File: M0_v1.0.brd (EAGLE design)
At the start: 68.6 x 53.3 mm, 61 parts, among them CN1 POWER_JACK, CN2 47346-0001, CN3 DIGITAL10, CN4 DIGITAL8, CN5 ICSP, CN6 POWER8, CN7 ANALOG6, CN8 SWD, CN9 UART, IC1 AMS1117-5.0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

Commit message: Moved i2c lines away from usb lines to prevent interference.
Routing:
- net SCL: track 38.2 -> 33.5 mm
- net SDA: track 36.2 -> 31.6 mm
- net GND: vias 210 -> 211
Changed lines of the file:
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@@
 <via x="43.053" y="35.687" extent="1-16" drill="0.35"/>
 <via x="43.053" y="27.94" extent="1-16" drill="0.35"/>
-<via x="39.497" y="25.527" extent="1-16" drill="0.35"/>
+<via x="39.624" y="25.527" extent="1-16" drill="0.35"/>
 <via x="33.909" y="28.194" extent="1-16" drill="0.35"/>
 <via x="49.657" y="6.604" extent="1-16" drill="0.35"/>
 <via x="18.923" y="36.195" extent="1-16" drill="0.35"/>
 <via x="29.464" y="31.877" extent="1-16" drill="0.35"/>
-<via x="38.354" y="32.385" extent="1-16" drill="0.35"/>
-<via x="34.036" y="34.671" extent="1-16" drill="0.35"/>
-<via x="22.606" y="46.355" extent="1-16" drill="0.35"/>
-<via x="22.86" y="41.402" extent="1-16" drill="0.35"/>
-<via x="28.702" y="39.624" extent="1-16" drill="0.35"/>
-<via x="34.163" y="39.624" extent="1-16" drill="0.35"/>
-<via x="28.067" y="46.355" extent="1-16" drill="0.35"/>
-<via x="18.923" y="39.751" extent="1-16" drill="0.35"/>
+<via x="37.465" y="31.369" extent="1-16" drill="0.35"/>
+<via x="34.798" y="32.004" extent="1-16" drill="0.35"/>
+<via x="25.273" y="46.228" extent="1-16" drill="0.35"/>
+<via x="29.464" y="41.656" extent="1-16" drill="0.35"/>
+<via x="29.845" y="37.084" extent="1-16" drill="0.35"/>
+<via x="34.671" y="36.576" extent="1-16" drill="0.35"/>
+<via x="30.861" y="46.228" extent="1-16" drill="0.35"/>
+<via x="19.812" y="40.005" extent="1-16" drill="0.35"/>
 <via x="18.923" y="46.228" extent="1-16" drill="0.35"/>
-<via x="18.034" y="48.387" extent="1-16" drill="0.35"/>
+<via x="18.034" y="48.514" extent="1-16" drill="0.35"/>
 <via x="14.605" y="39.878" extent="1-16" drill="0.35"/>
 <via x="10.795" y="35.941" extent="1-16" drill="0.35"/>
@@
 <wire x1="49.09495" y1="31" x2="48.9808" y2="31.11415" width="0.3048" layer="1"/>
 <via x="54.356" y="4.826" extent="1-16" drill="0.35"/>
-<via x="33.401" y="44.704" extent="1-16" drill="0.35"/>
+<via x="34.417" y="42.545" extent="1-16" drill="0.35"/>
 <via x="61.595" y="42.926" extent="1-16" drill="0.35"/>
 <via x="12.827" y="25.273" extent="1-16" drill="0.35"/>
@@
 <via x="37.338" y="49.276" extent="1-16" drill="0.35"/>
 <via x="57.531" y="48.26" extent="1-16" drill="0.35"/>
-<via x="22.86" y="48.514" extent="1-16" drill="0.35"/>
+<via x="24.892" y="41.656" extent="1-16" drill="0.35"/>
 <via x="18.288" y="21.844" extent="1-16" drill="0.35"/>
 <via x="22.098" y="24.257" extent="1-16" drill="0.35"/>
@@
 <via x="43.18" y="23.241" extent="1-16" drill="0.35"/>
 <via x="55.499" y="31.242" extent="1-16" drill="0.35"/>
+<via x="22.987" y="48.641" extent="1-16" drill="0.35"/>
 </signal>
 <signal name="VIN" class="3">
@@
 <wire x1="58.4736" y1="45.1386" x2="40.1828" y2="45.1386" width="0.254" layer="1"/>
 <wire x1="40.1828" y1="45.1386" x2="37.084" y2="48.2374" width="0.254" layer="1"/>
-<wire x1="37.084" y1="48.2374" x2="25.5086125" y2="48.2374" width="0.254" layer="1"/>
-<wire x1="25.5086125" y1="48.2374" x2="24.13" y2="49.6160125" width="0.254" layer="1"/>
-<wire x1="24.13" y1="49.6160125" x2="24.13" y2="50.8" width="0.254" layer="1"/>
+<wire x1="37.084" y1="48.2374" x2="25.3816125" y2="48.2374" width="0.254" layer="1"/>
+<wire x1="25.3816125" y1="48.2374" x2="24.13" y2="49.4890125" width="0.254" layer="1"/>
+<wire x1="24.13" y1="49.4890125" x2="24.13" y2="50.8" width="0.254" layer="1"/>
 </signal>
 <signal name="SCL">
@@
 <contactref element="U2" pad="32"/>
 <wire x1="43.463" y1="31" x2="42.613" y2="31" width="0.254" layer="1"/>
-<via x="20.701" y="39.545" extent="1-16" drill="0.35"/>
-<wire x1="42.613" y1="31" x2="35.1426625" y2="31" width="0.254" layer="1"/>
-<wire x1="35.1426625" y1="31" x2="26.7218625" y2="39.4208" width="0.254" layer="1"/>
-<wire x1="20.8252" y1="39.4208" x2="20.701" y2="39.545" width="0.254" layer="1"/>
-<wire x1="26.7218625" y1="39.4208" x2="20.8252" y2="39.4208" width="0.254" layer="1"/>
-<wire x1="20.701" y1="49.149" x2="19.05" y2="50.8" width="0.254" layer="16"/>
-<wire x1="20.701" y1="49.149" x2="20.701" y2="39.545" width="0.254" layer="16"/>
+<via x="22.479" y="45.895" extent="1-16" drill="0.35"/>
+<wire x1="42.613" y1="31" x2="39.184" y2="31" width="0.254" layer="1"/>
+<wire x1="39.184" y1="31" x2="38.06833125" y2="32.11566875" width="0.254" layer="1"/>
+<wire x1="38.06833125" y1="32.11566875" x2="36.25833125" y2="32.11566875" width="0.254" layer="1"/>
+<wire x1="36.25833125" y1="32.11566875" x2="22.479" y2="45.895" width="0.254" layer="1"/>
+<wire x1="22.479" y1="45.895" x2="20.828" y2="47.546" width="0.254" layer="16"/>
+<wire x1="20.828" y1="49.022" x2="19.05" y2="50.8" width="0.254" layer="16"/>
+<wire x1="20.828" y1="49.022" x2="20.828" y2="47.546" width="0.254" layer="16"/>
 </signal>
 <signal name="SDA">
@@
 <contactref element="U2" pad="31"/>
 <wire x1="43.463" y1="31.5" x2="42.613" y2="31.5" width="0.254" layer="1"/>
-<via x="21.59" y="40.0784" extent="1-16" drill="0.35"/>
-<wire x1="42.613" y1="31.5" x2="35.4714" y2="31.5" width="0.254" layer="1"/>
-<wire x1="35.4714" y1="31.5" x2="26.8902" y2="40.0812" width="0.254" layer="1"/>
-<wire x1="26.8902" y1="40.0812" x2="21.5928" y2="40.0812" width="0.254" layer="1"/>
-<wire x1="21.59" y1="40.0784" x2="21.5928" y2="40.0812" width="0.254" layer="1"/>
-<wire x1="21.59" y1="40.0784" x2="21.59" y2="50.8" width="0.254" layer="16"/>
+<via x="22.5806" y="46.8094" extent="1-16" drill="0.35"/>
+<wire x1="42.613" y1="31.5" x2="39.438" y2="31.5" width="0.254" layer="1"/>
+<wire x1="39.438" y1="31.5" x2="38.295" y2="32.643" width="0.254" layer="1"/>
+<wire x1="38.295" y1="32.643" x2="36.7414" y2="32.643" width="0.254" layer="1"/>
+<wire x1="22.5806" y1="46.8094" x2="22.5806" y2="46.8038" width="0.254" layer="1"/>
+<wire x1="36.7414" y1="32.643" x2="22.5806" y2="46.8038" width="0.254" layer="1"/>
+<wire x1="22.5806" y1="46.8094" x2="22.558" y2="46.8094" width="0.254" layer="16"/>
+<wire x1="22.558" y1="46.8094" x2="21.59" y2="47.7774" width="0.254" layer="16"/>
+<wire x1="21.59" y1="50.8" x2="21.59" y2="47.7774" width="0.254" layer="16"/>
 </signal>
 <signal name="A3">
@@
 <contactref element="U2" pad="13"/>
 <wire x1="49.613" y1="35.15" x2="49.613" y2="36" width="0.254" layer="1"/>
-<wire x1="51.645" y1="38.921" x2="49.613" y2="36.889" width="0.254" layer="1"/>
 <wire x1="49.613" y1="36" x2="49.613" y2="36.889" width="0.254" layer="1"/>
-<wire x1="55.626" y1="38.862" x2="55.567" y2="38.921" width="0.254" layer="1"/>
-<wire x1="55.567" y1="38.921" x2="51.645" y2="38.921" width="0.254" layer="1"/>
+<wire x1="55.626" y1="38.862" x2="51.586" y2="38.862" width="0.254" layer="1"/>
+<wire x1="51.586" y1="38.862" x2="49.613" y2="36.889" width="0.254" layer="1"/>
 <via x="55.626" y="38.862" extent="1-16" drill="0.35"/>
 <wire x1="53.34" y1="50.8" x2="55.626" y2="48.514" width="0.254" layer="16"/>
@@
 <wire x1="47.379" y1="21.082" x2="46.22" y2="21.082" width="0.254" layer="1"/>
 <via x="35.56" y="14.605" extent="1-16" drill="0.35"/>
-<wire x1="64.643" y1="14.605" x2="47.371" y2="14.605" width="0.254" layer="1"/>
+<wire x1="64.77" y1="14.605" x2="47.371" y2="14.605" width="0.254" layer="1"/>
 <wire x1="47.371" y1="14.605" x2="35.56" y2="14.605" width="0.254" layer="1"/>
 <wire x1="47.379" y1="21.082" x2="47.379" y2="20.074" width="0.254" layer="1"/>
@@
 <wire x1="47.371" y1="20.066" x2="47.371" y2="14.605" width="0.254" layer="16"/>
 <contactref element="CN8" pad="10"/>
-<wire x1="64.643" y1="14.605" x2="65.532" y2="15.494" width="0.254" layer="1"/>
+<wire x1="65.532" y1="15.367" x2="65.532" y2="15.494" width="0.254" layer="1"/>
+<wire x1="65.532" y1="15.367" x2="64.77" y2="14.605" width="0.254" layer="1"/>
 <wire x1="66.4083" y1="21.8567" x2="63.627" y2="24.638" width="0.254" layer="16"/>
 <wire x1="63.627" y1="24.638" x2="63.627" y2="25.4" width="0.254" layer="16"/>

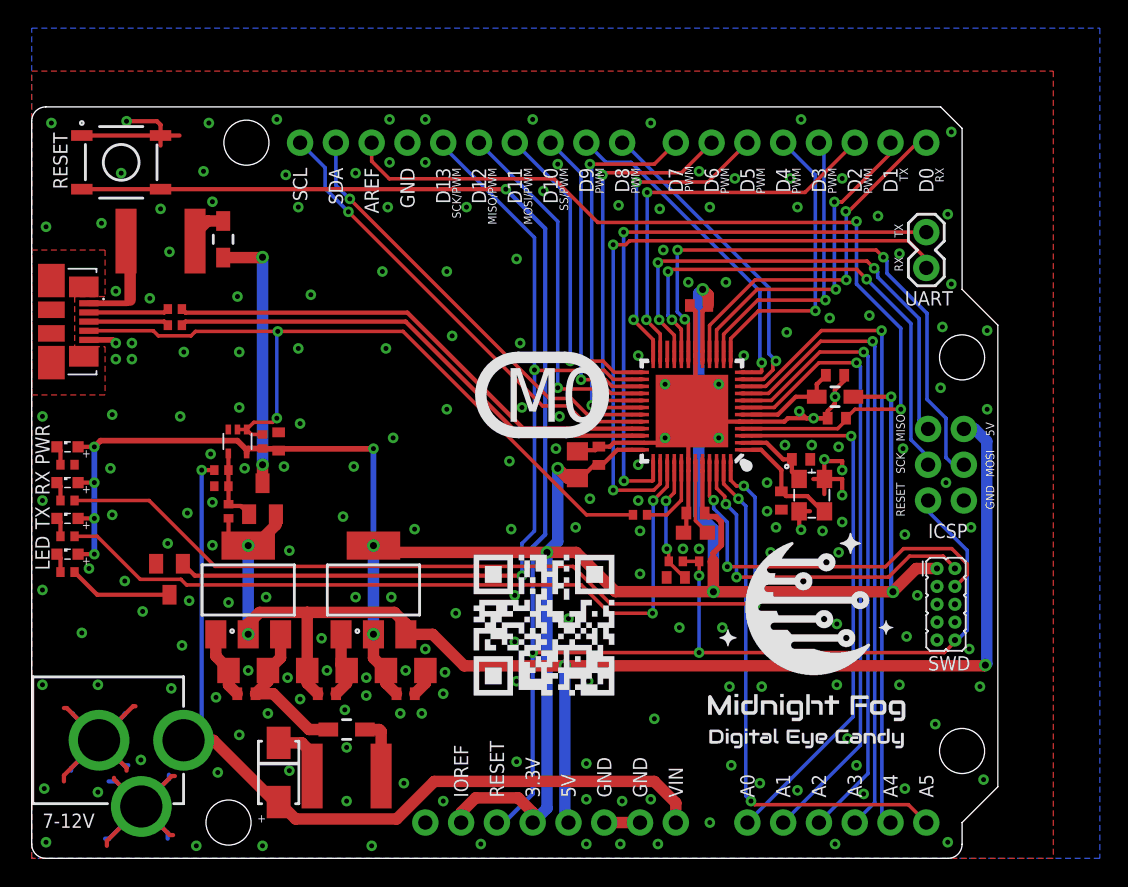
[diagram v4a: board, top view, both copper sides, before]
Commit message: Moved few traces around.
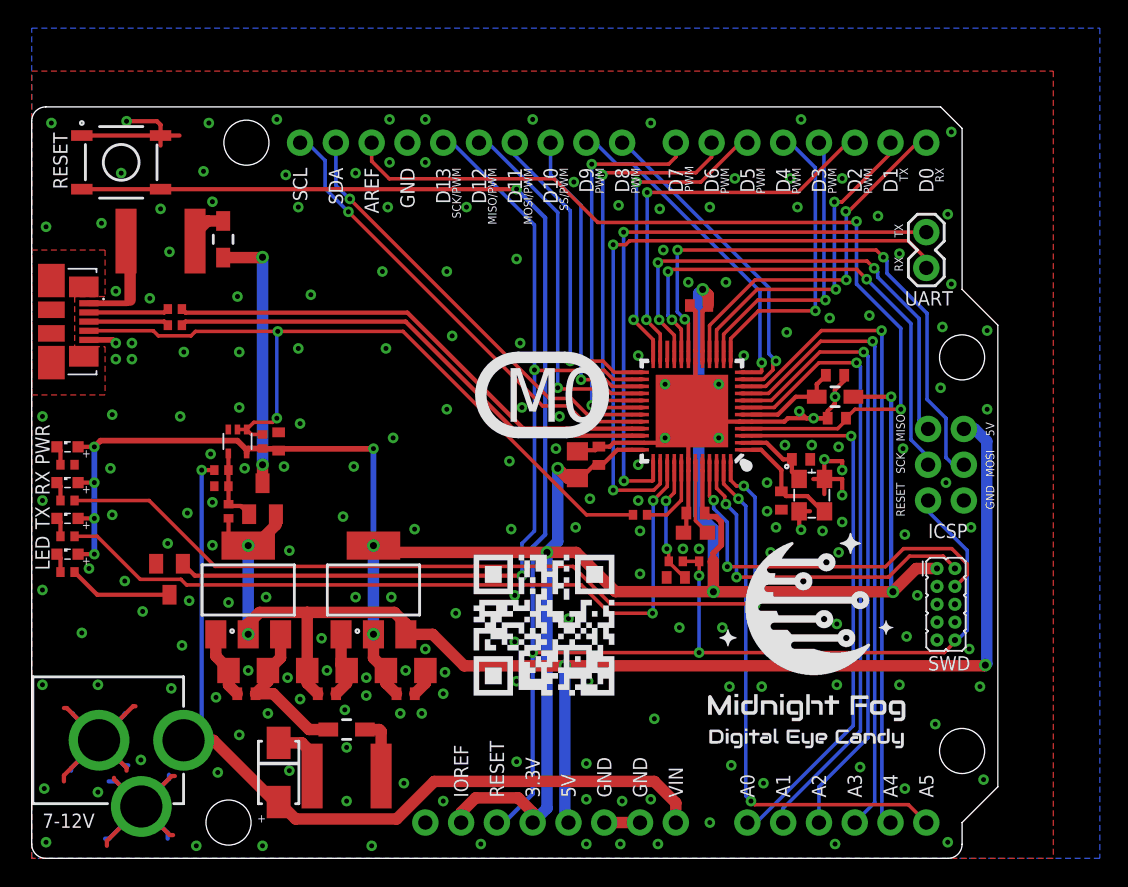
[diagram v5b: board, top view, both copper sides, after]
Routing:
- net D6_PWM: track 27.6 -> 28.1 mm
- net GND: vias 211 -> 206

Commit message: Moved few components around.
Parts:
- moved C12 0.25 mm to (53.2, 25.1)
- moved C13 0.18 mm to (54.7, 28.2)
- moved Q2 0.13 mm to (55.4, 25.7)
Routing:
- net GND: track 120.2 -> 121.5 mm, vias 206 -> 205
